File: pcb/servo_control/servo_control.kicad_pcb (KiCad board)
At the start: 2 copper layers, 94.6 x 62.9 mm, 50 parts, among them J1 USB_B_Micro, J10 Conn_01x03_Female, J11 Conn_01x03_Female, J12 Conn_01x03_Female, J13 Conn_01x03_Female, J14 Conn_01x03_Female, J15 Conn_01x03_Female, J16 Conn_01x03_Female, J17 Conn_01x03_Female, J18 Conn_01x03_Female, J19 Conn_01x03_Female, J2 YLIDAR X4, J20 Conn_01x03_Female, J21 Conn_01x06_Male, J3 Conn_01x03_Female, J4 Conn_01x03_Female, J5 Conn_01x03_Female, J6 Conn_01x03_Female, J7 Conn_01x03_Female, J8 Conn_01x03_Female, J9 Conn_01x03_Female, SW1 ESP_PROG, SW2 ESP_RST, U1 PCA9685BS, U2 LM317_SOT-223, U3 ESP32-WROOM-32, U4 MPU-9250, U5 PCA9685BS

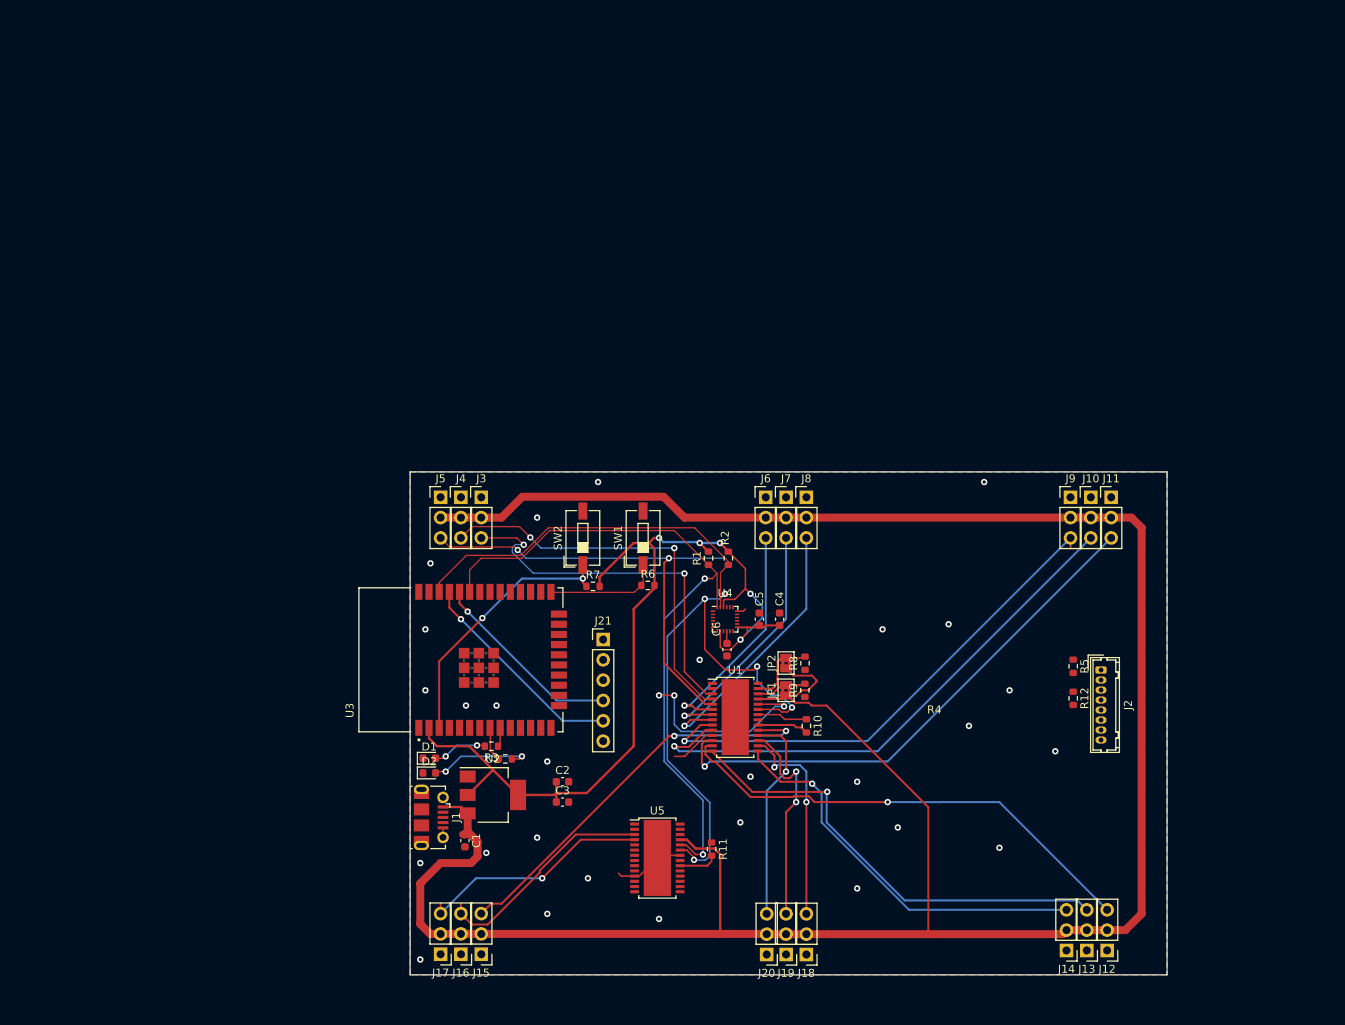
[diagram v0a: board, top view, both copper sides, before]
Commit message: add dual cell charger
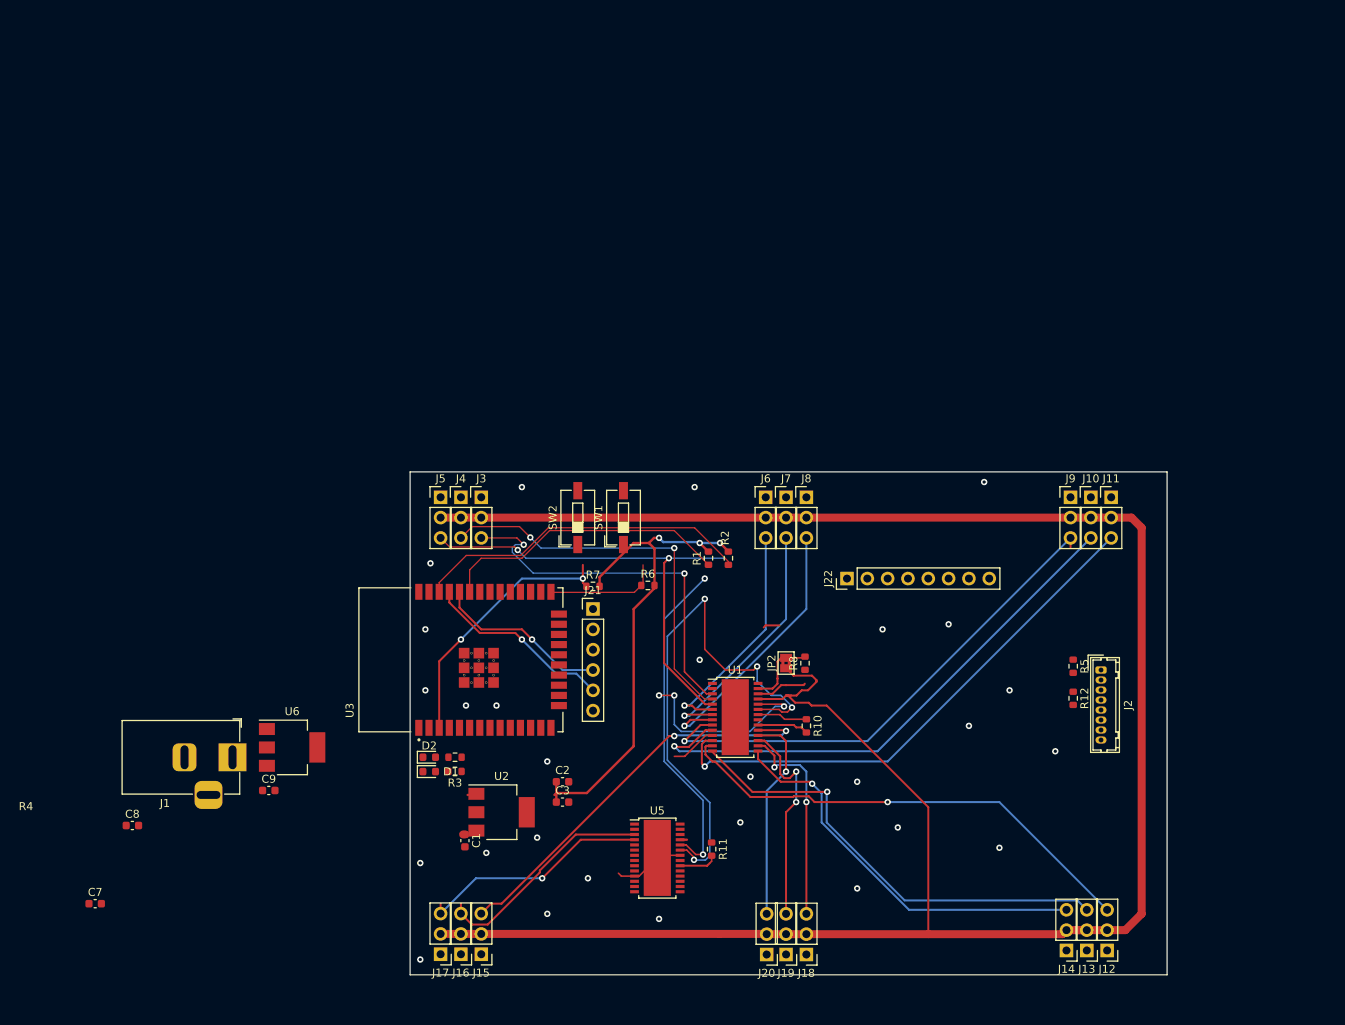
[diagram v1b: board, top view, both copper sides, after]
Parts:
- removed C4: 10 nf, Capacitor_SMD:C_0603_1608Metric
- removed C5, C6: 0.1 uf, Capacitor_SMD:C_0603_1608Metric
- removed JP1: Jumper_2_Open, Jumper:SolderJumper-2_P1.3mm_Bridged2Bar_Pad1.0x1.5mm
- removed R9: 10K, Resistor_SMD:R_0603_1608Metric
- removed U4: MPU-9250, Sensor_Motion:InvenSense_QFN-24_3x3mm_P0.4mm
- added C7: 1 uf, Capacitor_SMD:C_0603_1608Metric, F.Cu at (61.0, 94.0)
- added C8: 1uf, Capacitor_SMD:C_0603_1608Metric, F.Cu at (65.6, 84.2)
- added C9: 10 uf, Capacitor_SMD:C_0603_1608Metric, F.Cu at (82.7, 79.8)
- added J22: GY-87, Connector_PinHeader_2.54mm:PinHeader_1x08_P2.54mm_Vertical, F.Cu at (154.9, 53.3)
- added U6: LM317-5_SOT-223, Package_TO_SOT_SMD:SOT-223-3_TabPin2, F.Cu at (85.6, 74.5)
- J1: value USB_B_Micro -> Jack-DC; footprint Connector_USB:USB_Micro-B_Molex-105017-0001 -> Connector_BarrelJack:BarrelJack_Horizontal
- U2: value LM317_SOT-223 -> LM317-3.3_SOT-223
- moved J1 26.0 mm to (78.1, 75.7), turned to 0 degrees
- moved R4 6.29 mm to (105.9, 75.7), turned to 180 degrees
- moved R3 5.54 mm to (105.9, 77.4)
- moved J21 4.02 mm to (123.2, 57.1)
- moved SW1 3.53 mm to (127.0, 45.7)
- moved SW2 2.62 mm to (121.3, 45.7)
- moved U2 2.42 mm to (111.8, 82.5)
- moved D2 1.97 mm to (102.7, 75.7)
- moved D1 1.67 mm to (102.7, 77.5)
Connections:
- C1 pad 1: VCC -> 9V
- J1 pad 1: VCC -> 9V
- J1 pad 2: unconnected-(J1-Pad2) -> GND
- J1 pad 3: unconnected-(J1-Pad3) -> (no net)
- U1 pad 25: VCC -> 5V
- U2 pad 3: VCC -> 9V
- U5 pad 25: VCC -> 5V
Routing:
- net 3.3V: track 118.1 -> 65.4 mm, vias 5 -> 3
- net VCC: track 324.3 -> 279.8 mm
- net Net-(D2-Pad2): track 13.0 -> 0.00 mm, vias 2 -> 0
- net I2C_SCL: track 118.7 -> 109.6 mm, vias 5 -> 4
- net I2C_SDA: track 111.8 -> 103.3 mm
- net Net-(D1-Pad2): track 6.87 -> 0.00 mm, vias 2 -> 0
- net LED_2: track 4.34 -> 0.08 mm
- net FTDI_RX: track 27.1 -> 23.8 mm
- net FTDI_TX: track 24.4 -> 21.9 mm
- net LED_1: track 2.40 -> 0.00 mm
- net GND: track 23.7 -> 21.4 mm
- net Net-(C6-Pad1): track 1.64 -> 0.00 mm
- net 5V: track 0.00 -> 0.85 mm
- removed copper zone on B.Cu, net GND
- removed copper zone on F.Cu, net GND

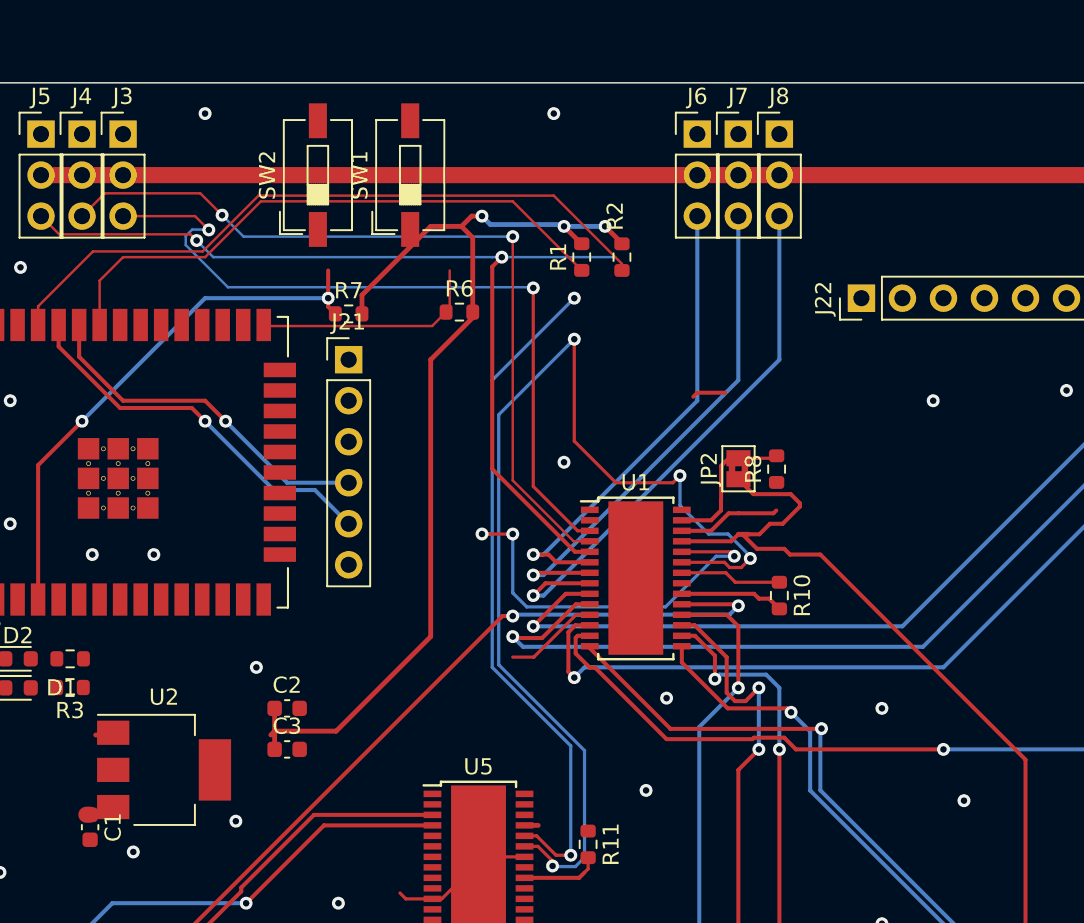
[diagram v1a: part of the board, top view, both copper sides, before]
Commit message: add lipo 2S charger
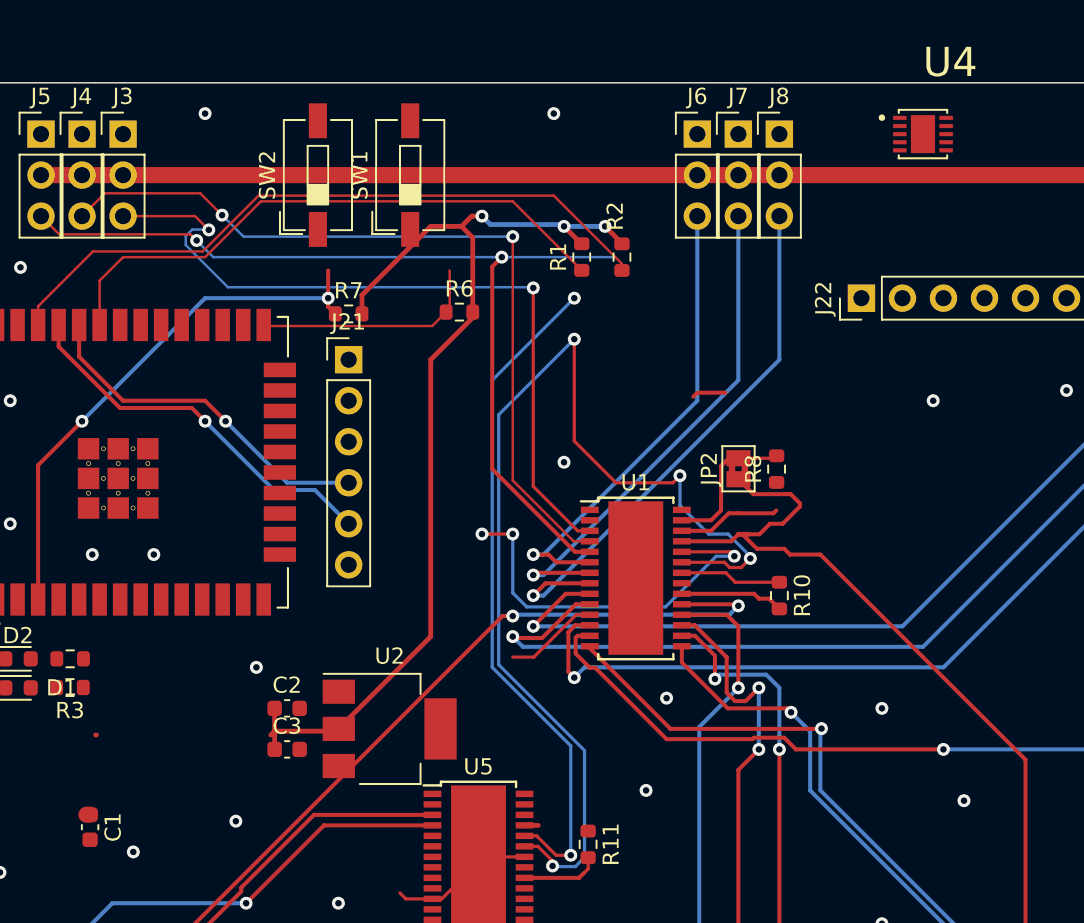
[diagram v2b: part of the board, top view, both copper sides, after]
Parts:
- added U4: MCP73213-A6SI/MF, MCP73213:SON50P300X300X100-11N, F.Cu at (158.8, 43.2)
- moved U2 14.2 mm to (125.7, 80.0)
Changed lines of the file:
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@@
   (net 84 "INTA")
   (net 85 "DRDY")
+  (net 86 "Net-(U4-Pad1)")
+  (net 87 "Net-(U4-Pad3)")
+  (net 88 "unconnected-(U4-Pad7)")
+  (net 89 "unconnected-(U4-Pad10)")
+  (net 90 "unconnected-(U4-Pad11)")
   (footprint "Capacitor_SMD:C_0603_1608Metric" (layer "F.Cu")
     (at 107.18 86.1 -90)
@@
     )
   )
+  (footprint "MCP73213:SON50P300X300X100-11N" (layer "F.Cu")
+    (at 158.75 43.18)
+    (property "AVAILABILITY" "Good")
+    (property "DESCRIPTION" "MCP Series 16V Dual-Cell Li-Ion/Li-Polymer Battery Charge Management Controller")
+    (property "MF" "Microchip")
+    (property "MP" "MCP73213-A6SI/MF")
+    (property "PACKAGE" "DFN-10 Microchip")
+    (property "PRICE" "1.60 USD")
+    (property "SNAPEDA_PACKAGE_ID" "30778")
+    (property "Sheetfile" "servo_control.kicad_sch")
+    (property "Sheetname" "")
+    (attr smd)
+    (fp_text reference "U4" (at 1.68851 -4.43234) (layer "F.SilkS")
+      (effects (font (size 1.807654 1.807654) (thickness 0.15)))
+    )
+    (fp_text value "MCP73213-A6SI/MF" (at 19.512085 4.589045) (layer "F.Fab")
+      (effects (font (size 1.795504 1.795504) (thickness 0.15)))
+    )
+    (fp_poly (pts
+        (xy -0.470575 -0.74)
+        (xy 0.47 -0.74)
+        (xy 0.47 0.740905)
+        (xy -0.470575 0.740905)
+      ) (layer "F.Paste") (width 0.01) (fill solid))
+    (fp_line (start 1.5 1.31) (end 1.5 1.5) (layer "F.SilkS") (width 0.127))
+    (fp_line (start 1.5 1.5) (end -1.5 1.5) (layer "F.SilkS") (width 0.127))
+    (fp_line (start -1.5 1.31) (end -1.5 1.5) (layer "F.SilkS") (width 0.127))
+    (fp_line (start -1.5 -1.5) (end 1.5 -1.5) (layer "F.SilkS") (width 0.127))
+    (fp_line (start 1.5 -1.5) (end 1.5 -1.31) (layer "F.SilkS") (width 0.127))
+    (fp_line (start -1.5 -1.5) (end -1.5 -1.31) (layer "F.SilkS") (width 0.127))
+    (fp_circle (center -2.54 -1.016) (end -2.44 -1.016) (layer "F.SilkS") (width 0.2) (fill none))
+    (fp_line (start 2.11 -1.8) (end 2.11 1.8) (layer "F.CrtYd") (width 0.05))
+    (fp_line (start -2.11 1.8) (end -2.11 -1.8) (layer "F.CrtYd") (width 0.05))
+    (fp_line (start 2.11 1.8) (end -2.11 1.8) (layer "F.CrtYd") (width 0.05))
+    (fp_line (start -2.11 -1.8) (end 2.11 -1.8) (layer "F.CrtYd") (width 0.05))
+    (fp_line (start -1.5 1.5) (end -1.5 -1.5) (layer "F.Fab") (width 0.127))
+    (fp_line (start -1.5 -1.5) (end 1.5 -1.5) (layer "F.Fab") (width 0.127))
+    (fp_line (start 1.5 1.5) (end -1.5 1.5) (layer "F.Fab") (width 0.127))
+    (fp_line (start 1.5 -1.5) (end 1.5 1.5) (layer "F.Fab") (width 0.127))
+    (fp_circle (center -2.54 -1.016) (end -2.44 -1.016) (layer "F.Fab") (width 0.2) (fill none))
+    (pad "1" smd roundrect locked (at -1.435 -1) (size 0.84 0.26) (layers "F.Cu" "F.Paste" "F.Mask") (roundrect_rratio 0.04)
+      (net 86 "Net-(U4-Pad1)") (pinfunction "VDD") (pintype "power_in"))
+    (pad "2" smd roundrect locked (at -1.435 -0.5) (size 0.84 0.26) (layers "F.Cu" "F.Paste" "F.Mask") (roundrect_rratio 0.04)
+      (net 86 "Net-(U4-Pad1)") (pinfunction "VDD") (pintype "power_in"))
+    (pad "3" smd roundrect locked (at -1.435 0) (size 0.84 0.26) (layers "F.Cu" "F.Paste" "F.Mask") (roundrect_rratio 0.04)
+      (net 87 "Net-(U4-Pad3)") (pinfunction "VBAT") (pintype "bidirectional"))
+    (pad "4" smd roundrect locked (at -1.435 0.5) (size 0.84 0.26) (layers "F.Cu" "F.Paste" "F.Mask") (roundrect_rratio 0.04)
+      (net 87 "Net-(U4-Pad3)") (pinfunction "VBAT") (pintype "bidirectional"))
+    (pad "5" smd roundrect locked (at -1.435 1) (size 0.84 0.26) (layers "F.Cu" "F.Paste" "F.Mask") (roundrect_rratio 0.04))
+    (pad "6" smd roundrect locked (at 1.435 1) (size 0.84 0.26) (layers "F.Cu" "F.Paste" "F.Mask") (roundrect_rratio 0.04))
+    (pad "7" smd roundrect locked (at 1.435 0.5) (size 0.84 0.26) (layers "F.Cu" "F.Paste" "F.Mask") (roundrect_rratio 0.04)
+      (net 88 "unconnected-(U4-Pad7)") (pinfunction "STAT") (pintype "output"))
+    (pad "8" smd roundrect locked (at 1.435 0) (size 0.84 0.26) (layers "F.Cu" "F.Paste" "F.Mask") (roundrect_rratio 0.04)
+      (net 1 "GND") (pinfunction "VSS") (pintype "power_in"))
+    (pad "9" smd roundrect locked (at 1.435 -0.5) (size 0.84 0.26) (layers "F.Cu" "F.Paste" "F.Mask") (roundrect_rratio 0.04)
+      (net 1 "GND") (pinfunction "VSS") (pintype "power_in"))
+    (pad "10" smd roundrect locked (at 1.435 -1) (size 0.84 0.26) (layers "F.Cu" "F.Paste" "F.Mask") (roundrect_rratio 0.04)
+      (net 89 "unconnected-(U4-Pad10)") (pinfunction "PROG") (pintype "bidirectional"))
+    (pad "11" smd rect locked (at 0 0) (size 1.5 2.35) (layers "F.Cu" "F.Mask")
+      (net 90 "unconnected-(U4-Pad11)") (pinfunction "EP") (pintype "power_in"))
+  )
   (footprint "Connector_Hirose:Hirose_DF13-08P-1.25DSA_1x08_P1.25mm_Vertical" (layer "F.Cu")
     (at 186.69 64.77 -90)
@@
   )
   (footprint "Package_TO_SOT_SMD:SOT-223-3_TabPin2" (layer "F.Cu")
-    (at 111.76 82.55)
+    (at 125.73 80.01)
     (descr "module CMS SOT223 4 pins")
     (tags "CMS SOT")
@@
       (effects (font (size 1 1) (thickness 0.15)))
     )
-    (fp_text user "${REFERENCE}" (at 0 0 90) (layer "F.Fab")
+    (fp_text user "${REFERENCE}" (at 0 -1.27 90) (layer "F.Fab")
       (effects (font (size 0.8 0.8) (thickness 0.12)))
     )
